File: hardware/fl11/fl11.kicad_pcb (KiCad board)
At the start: 2 copper layers, 282 x 20 mm, 67 parts, among them J1 USB-C 16P, J2_1 TOUCH_SENSE, J2_2 GND, J3_1 TOUCH_SENSE, J3_2 GND, Q1 AO3401A, SW1 BOOT, U1 ESP32-C3-MINI-1-N4, U2 SN74AHCT1G125, U3 AP2112K-3.3, U4 USBLC6-2SC6

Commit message: FL-11 rev B: electronics into a rear bulge, cable enters from the back
The LED row is untouched -- eleven at 16.66667 mm pitch, continuous, nothing
breaking the lit line. Everything else moved off the strip into a 48 x 28 mm
bulge below the middle, with the USB-C on the underside so the plug goes in
from the back.

Deleting the old 56 mm head nearly pays for the bulge: 5640 -> 5904 mm2,
+4.7%. The antenna comes out better than it was, at 21.9 mm from the nearest
LED copper against a rule of 8. The costs are honest ones: one bottom-side
part means a second assembly setup, about +$0.63/unit at qty 100, and the
outline is no longer a plain rectangle so the 6-up panel needs re-nesting.

Two electrical consequences the move forces:

- R11 goes 47R -> 100R. Section 6.6 sized 47R for a 12 mm buffer-to-LED1 run
  and argued it was electrically short. That run is now ~80 mm, past the
  doc's own ~75 mm critical length, so it needs real series termination.
- SENSE cannot use the y=1.4 channel any more: it must cross the LED data
  channel, and every x between LEDs carries a hop. It runs in a guarded
  y=18.6 lane and climbs at x=188, past LD11_DOUT's end at 186 -- the only
  place it can cross with no hop present.

Silkscreen now carries the lamp name, FL-11 rev B, the designer and the repo
URL, with the rev repeated on the tab so a snapped-off pad stays identified.

DRC 0 errors. 56 connections in the bulge remain unrouted; hardware README
says so and lists them.

Co-Authored-By: Claude Opus 5 (1M context) <noreply@anthropic.com>
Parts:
- J1: moved to B.Cu
- R11: value 47R -> 100R
- moved H2 103.6 mm to (114.0, 43.0)
- moved TP10 85.2 mm to (108.5, 44.5)
- moved U3 84.5 mm to (116.0, 25.0)
- moved R2 82.1 mm to (85.5, 38.5)
- moved R1 82.0 mm to (83.0, 38.5)
- moved J1 81.9 mm to (80.0, 45.0), turned to 180 degrees
- moved F1 80.6 mm to (98.0, 23.0)
- moved C3 79.5 mm to (110.0, 25.5)
- moved C2 79.1 mm to (110.0, 30.5)
- moved C7 79.1 mm to (112.5, 22.0)
- moved TP11 78.8 mm to (93.5, 21.5)
- moved TP9 78.1 mm to (108.5, 42.0)
- moved TP8 77.6 mm to (108.5, 39.5)
- moved Q1 77.2 mm to (105.0, 23.0)
- moved R8 77.1 mm to (110.0, 22.0)
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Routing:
- net LED_DIN1: track 8.29 -> 120.8 mm
- net TOUCH_SENSE: track 211.2 -> 120.7 mm
- net LED_DATA_5V: track 1.65 -> 3.04 mm
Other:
- board size 282 x 20 mm -> 228 x 48 mm
- board text added: "FL-11 rev B"
- board text added: "FL-11 rev B · Fionn Ferreira"
- board text added: "LINKED FRIEND LIGHTS"
- board text added: "LINKED FRIEND LIGHTS · FL-11 rev B · Fionn Ferreira"
- board text added: "github.com/fionnf/linked-friend-lights-public"

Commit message: FL-11 rev C: touch terminals join the electronics in the middle
The touch pad was a break-away tab at the far end, which meant SENSE -- a
high-impedance node the design calls its least-certain subsystem -- ran the
length of a strip carrying a 0.89 A switching rail. Moving the pad to a
snap-off section beside the bulge cuts that run from ~70 mm to ~13 mm, keeps
it inside the bulge's GND pour, and stops it crossing the LED data channel.

That crossing was the awkward part of rev B: every x between LEDs carries a
DOUT-to-DIN hop, so the only legal crossing point was x=188, past
LD11_DOUT's end. Both the guarded y=18.6 lane and that climb are now gone.

Deleting the end tab shortens the strip from 228 to 187 mm, so despite
gaining a pad section the board gets smaller: 5904 -> 5784 mm2, and only
2.6% above the original rev A while carrying rear-entry USB-C and a
continuous eleven-LED row.

Electrodes are 17 x 12 mm, 204 mm2 each -- the area section 7.5 asks for,
reproportioned for a pad section that is tall rather than long.

Every wire now leaves the lamp from one place. DRC 0 errors; 51 connections
in the bulge remain unrouted.

Co-Authored-By: Claude Opus 5 (1M context) <noreply@anthropic.com>
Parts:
- moved J2_2 79.3 mm to (117.5, 41.0)
- moved J3_2 77.9 mm to (128.0, 41.0)
- moved J2_1 76.0 mm to (117.5, 28.0)
- moved J3_1 74.5 mm to (128.0, 28.0)
- moved TP4 73.9 mm to (122.5, 44.5)
- moved TP7 3.91 mm to (183.0, 15.5)
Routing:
- net TOUCH_SENSE: track 120.7 -> 26.0 mm
- net GND: track 11.0 -> 12.5 mm, vias 11 -> 16
- net LD11_DOUT: track 12.1 -> 11.6 mm
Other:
- board size 228 x 48 mm -> 187 x 48 mm
- board text removed: "FL-11 rev B"
- board text removed: "FL-11 rev B · Fionn Ferreira"
- board text removed: "LINKED FRIEND LIGHTS"
- board text removed: "LINKED FRIEND LIGHTS · FL-11 rev B · Fionn Ferreira"
- board text removed: "github.com/fionnf/linked-friend-lights-public"

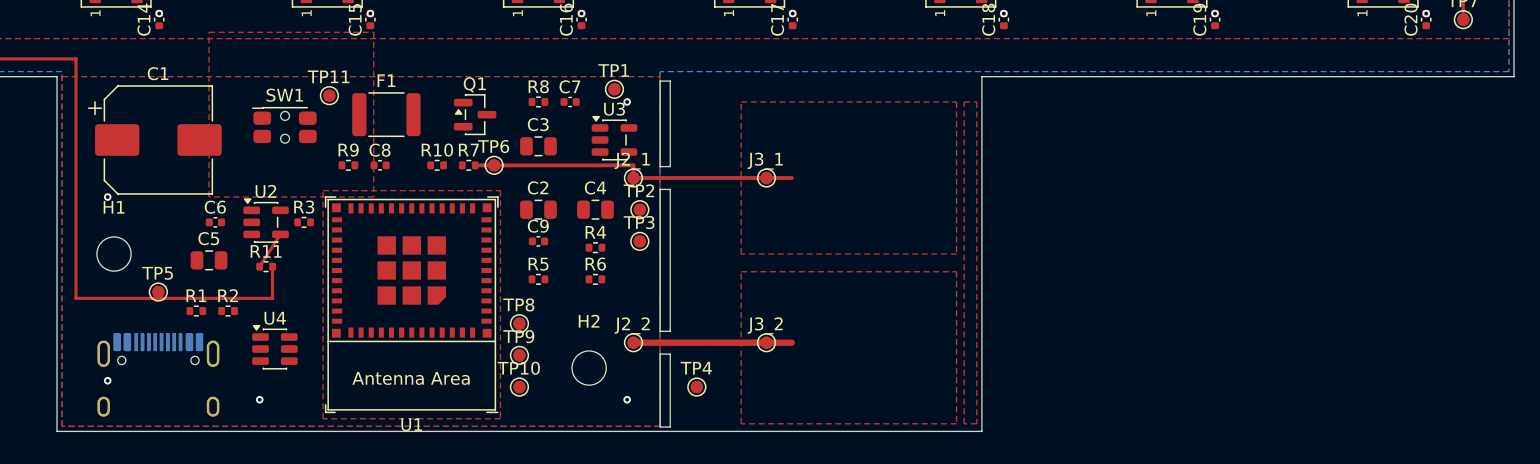
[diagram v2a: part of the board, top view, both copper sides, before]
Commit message: FL-11 rev D: single-sided, a break that actually breaks, real part numbers
Three fixes, each from something that was wrong.

J1 goes back to the top side. It is a horizontal receptacle, so the plug
enters along the board plane from the rear edge whichever face it sits on --
bottom-mounting bought flushness and cost a second assembly setup for it.
Rear entry is unchanged and the CPL now has zero bottom-side parts, so the
~$0.63/unit second-setup charge is gone.

The touch pad could not have been snapped off. It touched the rest of the
board on two edges, the bulge at x=120 and the strip along y=20, and only the
first was cut. The strip is now notched away over y 20-22 so the pad hangs
off the bulge alone, cantilevered where a hand can grip it, retained by two
1.3 mm webs and two 0.4 mm ligaments. Webs are 1.3 mm and not thinner because
a 0.30 mm trace needs 0.5 mm to each routed edge.

The BOM carries verified LCSC numbers. Blank part numbers are what made JLC
guess, and its guess for the 100k line was C880433: an 01005 part, Extended,
6 in stock, MOQ 5597. Every line is now filled from a live stock check.

Two lines are deliberately not filled. F1's PPTC could not be verified, so it
is blank rather than invented, and the LED C5378724 is carried over unverified
and flagged -- it is section 9.1's number one live risk.

Two costs went up and should be said plainly: the module quotes $3.84 against
the $2.92 modelled, and more Extended lines raise the fixed assembly charge by
roughly $0.30/board at qty 30.

DRC 0 errors. 51 connections in the bulge remain unrouted.

Co-Authored-By: Claude Opus 5 (1M context) <noreply@anthropic.com>
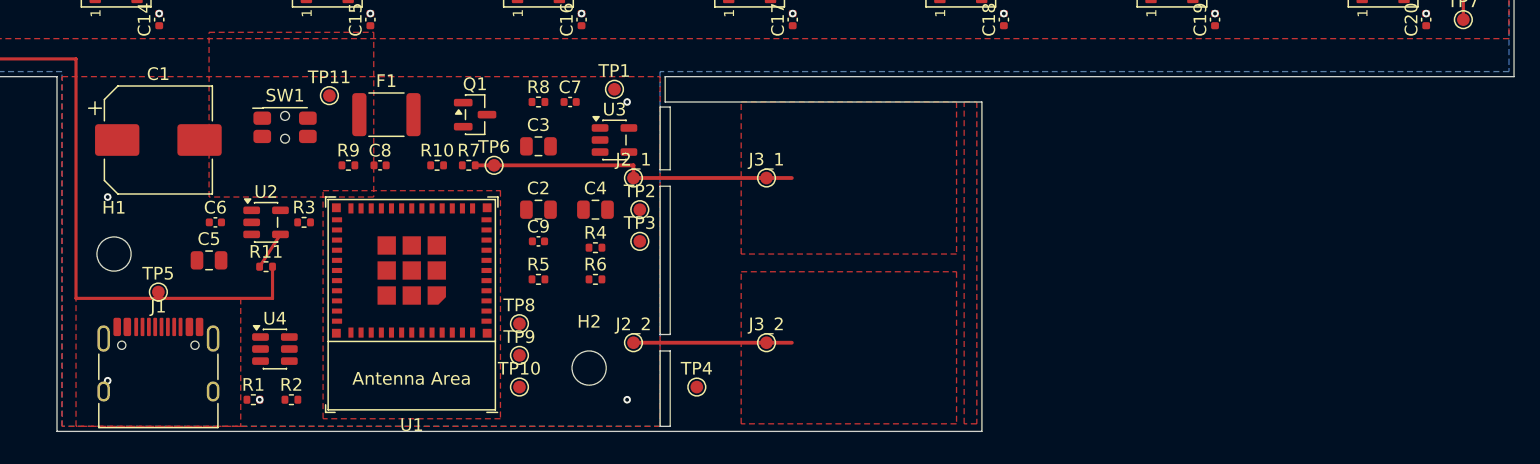
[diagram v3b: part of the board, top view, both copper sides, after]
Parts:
- J1: moved to F.Cu
- moved R2 8.60 mm to (90.5, 45.5)
- moved R1 8.32 mm to (87.5, 45.5)
- moved J1 1.20 mm to (80.0, 43.8), turned to 0 degrees
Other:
- outline, holes or cut-outs redrawn
